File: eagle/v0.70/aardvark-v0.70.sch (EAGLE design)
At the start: 22 parts, among them IC1 LM1117-3.3, J1 USB_MINI-B_SMT, U1 CH340C

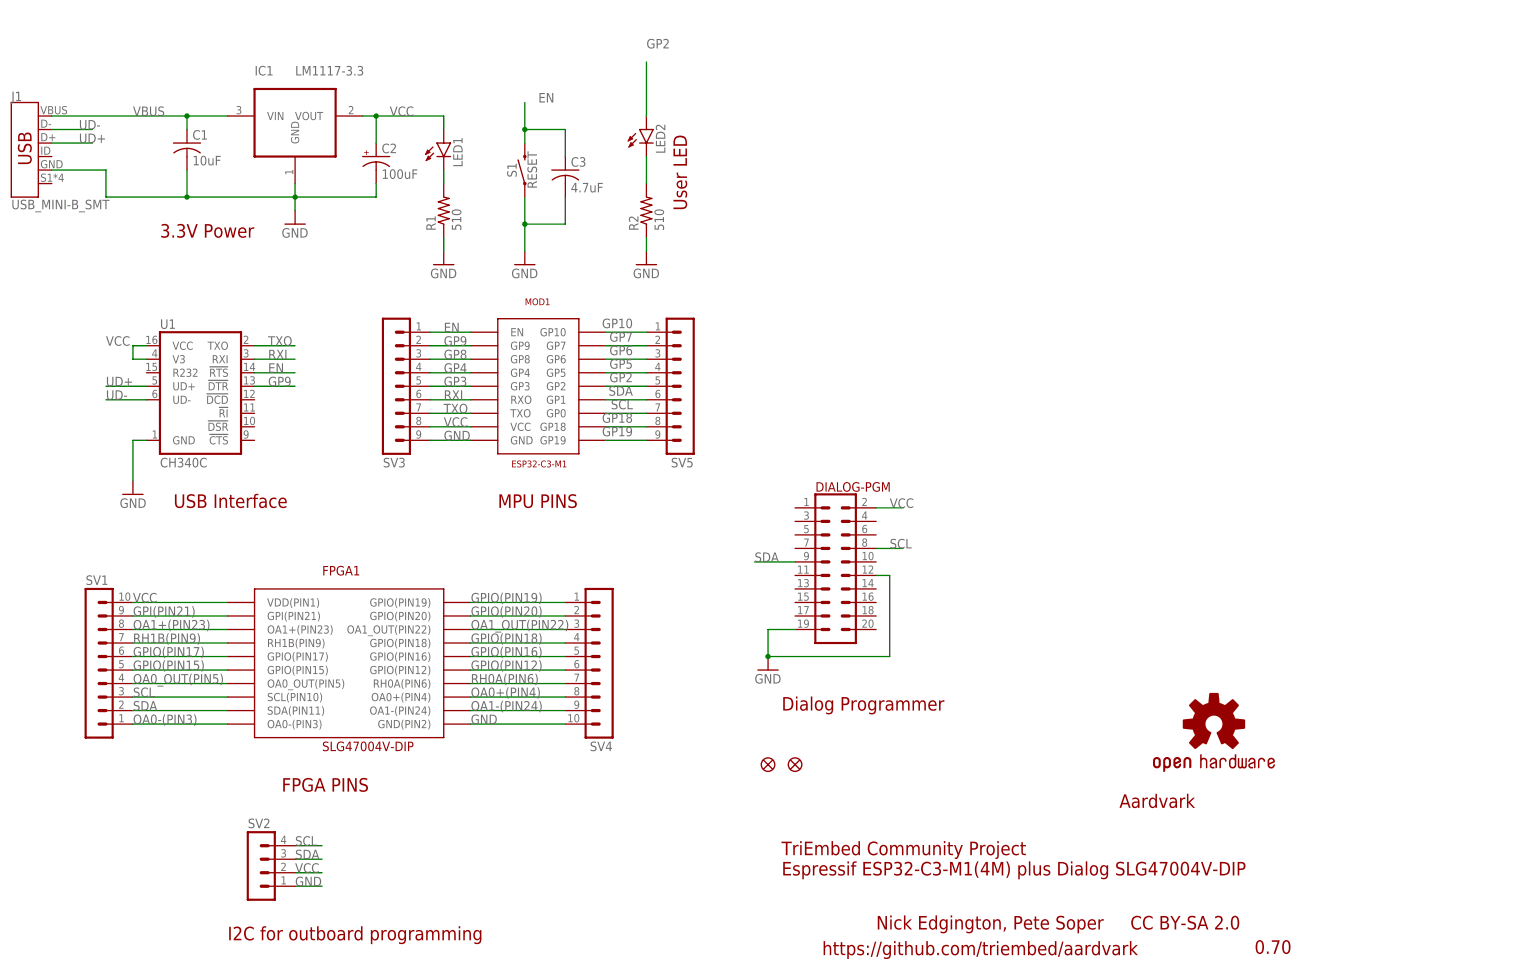
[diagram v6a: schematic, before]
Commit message: Finished initial ECOs for 0.70 board
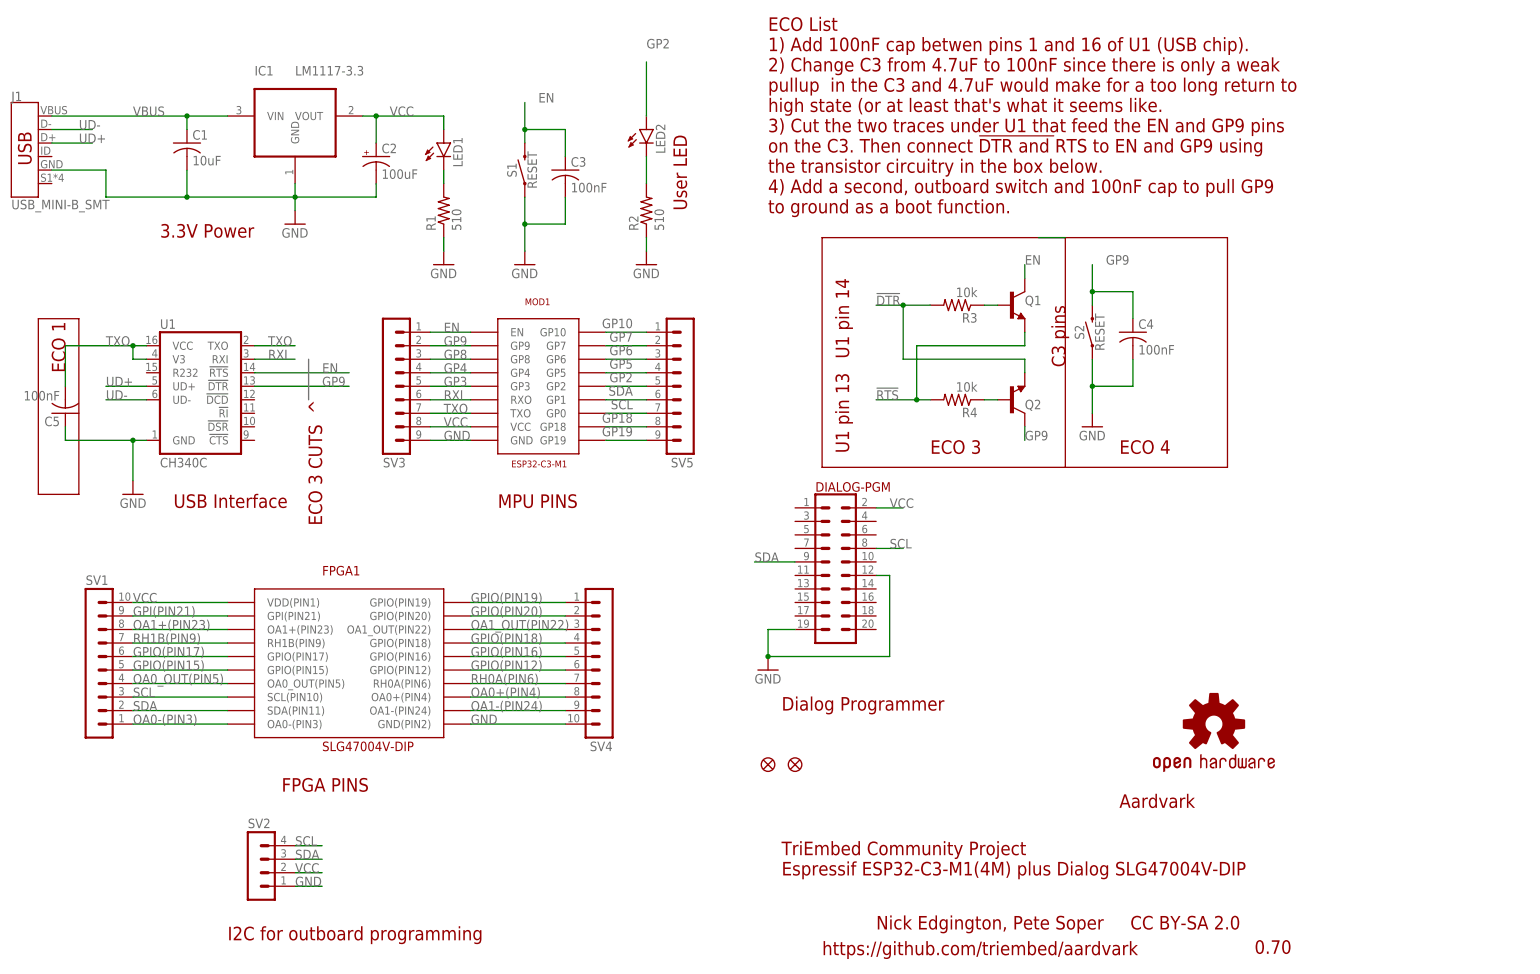
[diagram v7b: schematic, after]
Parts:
- added C4, C5: 100nF, rcl:C-USC0805
- added Q1, Q2: TRANS_NPN-MMBT2222AL, SparkFun-DiscreteSemi:TRANS_NPN-MMBT2222AL
- added R3, R4: 10k, rcl:R-US_R0805
- added S2: RESET, SparkFun-Switches:MOMENTARY-SWITCH-SPST-SMD-6.0X3.5MM
- C3: value 4.7uF -> 100nF
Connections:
- new net !DTR: Q2.E, R3.2
- new net !RTS: Q1.E, R4.2
- new net N$10: Q1.B, R3.1
- new net N$11: Q2.B, R4.1
- net EN: now also Q1.C
- net GND: now also C4.2, C5.1, S2.1
- net GP9: now also C4.1, Q2.C, S2.2
- net TXO: now also C5.2, U1.V3, U1.VCC
- net VCC: no longer U1.V3, U1.VCC
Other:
- note added: "C3 pins"
- note added: "ECO 1"
- note added: "ECO 3"
- note added: "ECO 3 CUTS ^"
- note added: "ECO 4"
- note added: "ECO List 1) Add 100nF cap betwen pins 1 and 16 of U1 (USB chip). 2) Change C3 from 4.7uF to 100nF since there is only a weak pullup in the C3 and 4.7uF would make for a too long return to high state (or at least that's what it seems like. 3) Cut the two traces under U1 that feed the EN and GP9 pins on the C3. Then connect !DTR and !RTS to EN and GP9 using the transistor circuitry in the box below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"
- note added: "U1 pin 13"
- note added: "U1 pin 14"
